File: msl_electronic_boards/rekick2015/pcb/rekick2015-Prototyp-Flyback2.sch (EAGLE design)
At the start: 207 parts, among them IC1 74LVC1G02GW, IC2 4043D, IC3 LM1117, IC4 LM1458D, Q1 16MHz, Q2 IGW60T120, Q3 PSMN7R8-120PS, Q4 PSMN7R8-120PS, Q5 IPD90P04P4L, Q6 IRF840, T1 BC859, T2 BC849, T3 BC849, T4 BC849, T5 IRLML6344TRPBF, U1 TXB0108PWR, U3 LM2675, U4 LM2675, U5 ADUM4190BRIZ, U6 ADUM4190BRIZ

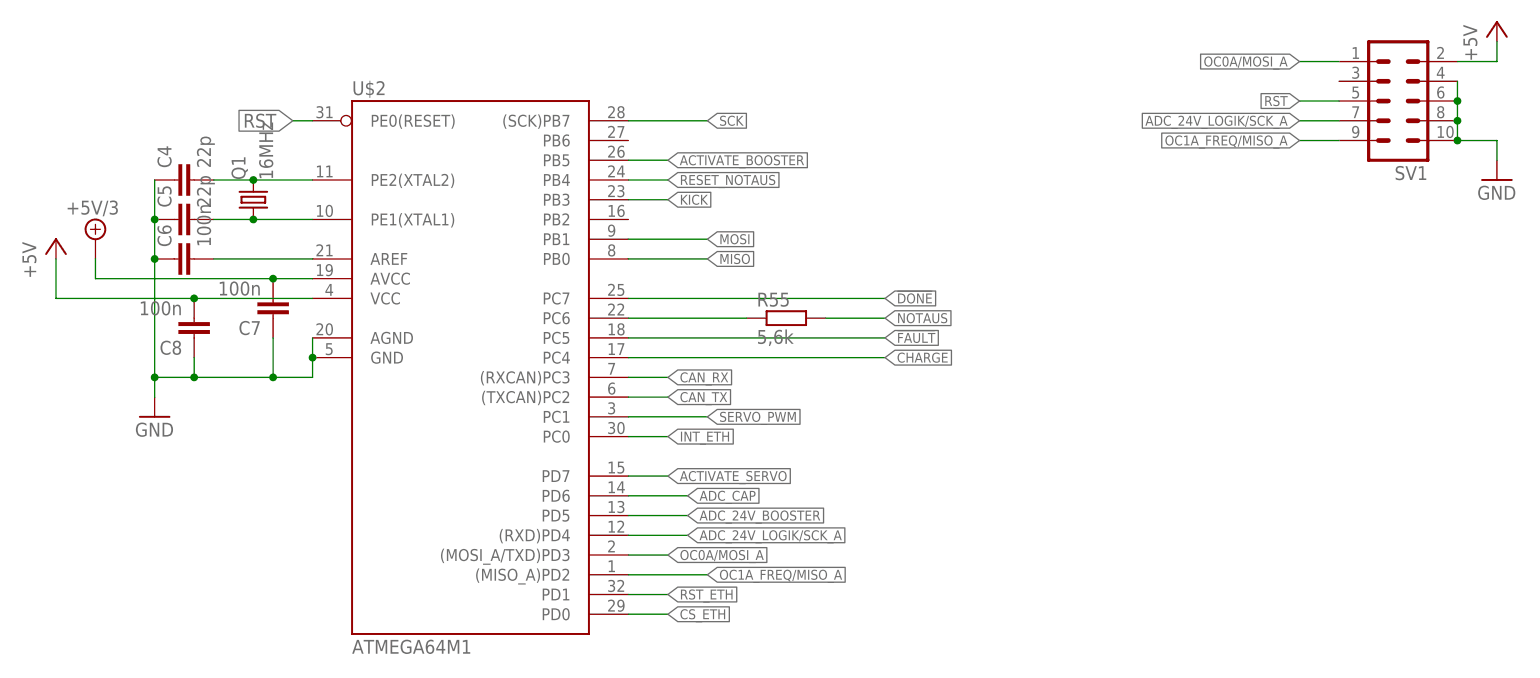
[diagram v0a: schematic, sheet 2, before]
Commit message: rekick flyback layout
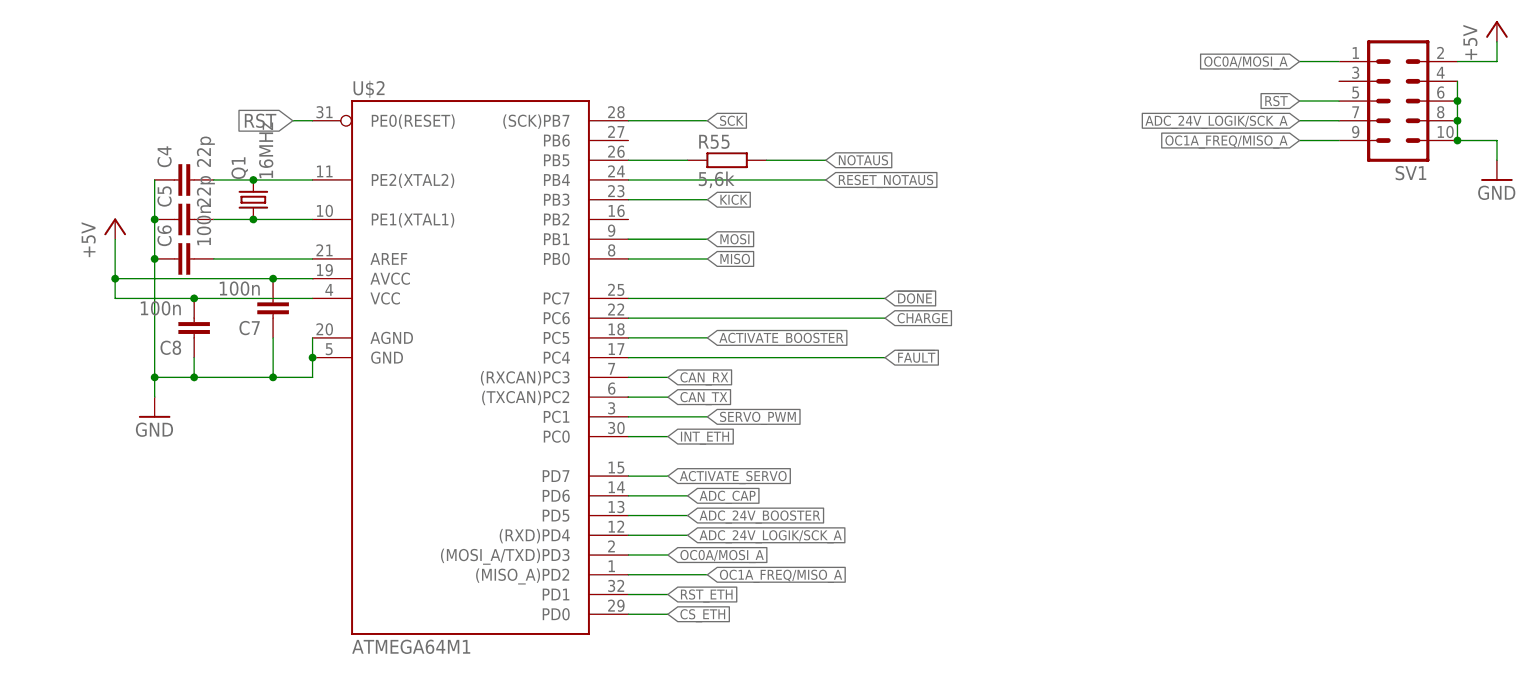
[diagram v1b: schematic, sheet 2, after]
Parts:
- removed R21, R25: 1k, rcl:R-EU_R0805
- removed R26, R29: 100k, rcl:R-EU_R0805
- added KK4: SK104, heatsink:SK104
- added R7, R8: 5,6k, rcl:R-EU_R0805
- JP3: device pinhead:PINHD-1X3 -> pinhead:PINHD-1X3/90
- R61, R67: value 40.2k -> 80.6k
- R62: value 18.2k -> 36.5k
- R69: value 50k -> 10k
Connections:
- removed net N$51: R55.1, U$2.PC6
- removed net N$82: R21.2, R26.2, U6.+IN
- removed net N$83: R29.1, U6.COMP
- removed net N$84: C47.1, R25.1, U6.REFOUT2
- new net N$12: JP4.1, R8.2
- new net N$13: R55.1, U$2.PB5
- new net N$2: JP3.1, R7.2
- net !FAULT: now also U$2.PC4; no longer U$2.PC5
- net +5V: now also C7.2, U$2.AVCC
- net +5V/3: now also IC4B.-IN; no longer C7.2, IC4A.-IN, U$2.AVCC
- net ACTIVATE_BOOSTER: now also U$2.PC5; no longer U$2.PB5
- net ADC_CAP_OV: now also IC4B.+IN; no longer IC4A.+IN
- net CAP_0V: now also H2.MOUNT; no longer H1.MOUNT, R26.1, R38.1, VR2.A, VR3.A
- net CHARGE: now also U$2.PC6; no longer U$2.PC4
- net GND: now also H1.MOUNT, R38.1, VR2.A, VR3.A; no longer H2.MOUNT
- net N$27: now also U6.+IN; no longer R21.1
- net N$85: now also C47.1, U6.REFOUT2; no longer R25.2, R29.2
- net OC0A/MOSI_A: now also R8.1; no longer JP4.1
- net SERVO_PWM: now also R7.1; no longer JP3.1
- net ÜBERSPANNUNG: now also IC4B.OUT; no longer IC4A.OUT
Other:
- moved on the sheet: H1, H2, R55
